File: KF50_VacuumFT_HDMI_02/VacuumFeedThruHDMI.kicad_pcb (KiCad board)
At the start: 4 copper layers, 112 x 151.5 mm, 16 parts, among them J1 HDMI_A_1.4, J2 HDMI_A_1.4, J3 HDMI_A_1.4, J4 HDMI_A_1.4, J5 HDMI_A_1.4, J6 HDMI_A_1.4, J7 HDMI_A_1.4, J8 HDMI_A_1.4, J9 HDMI_A_1.4, M1 DB25_Male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

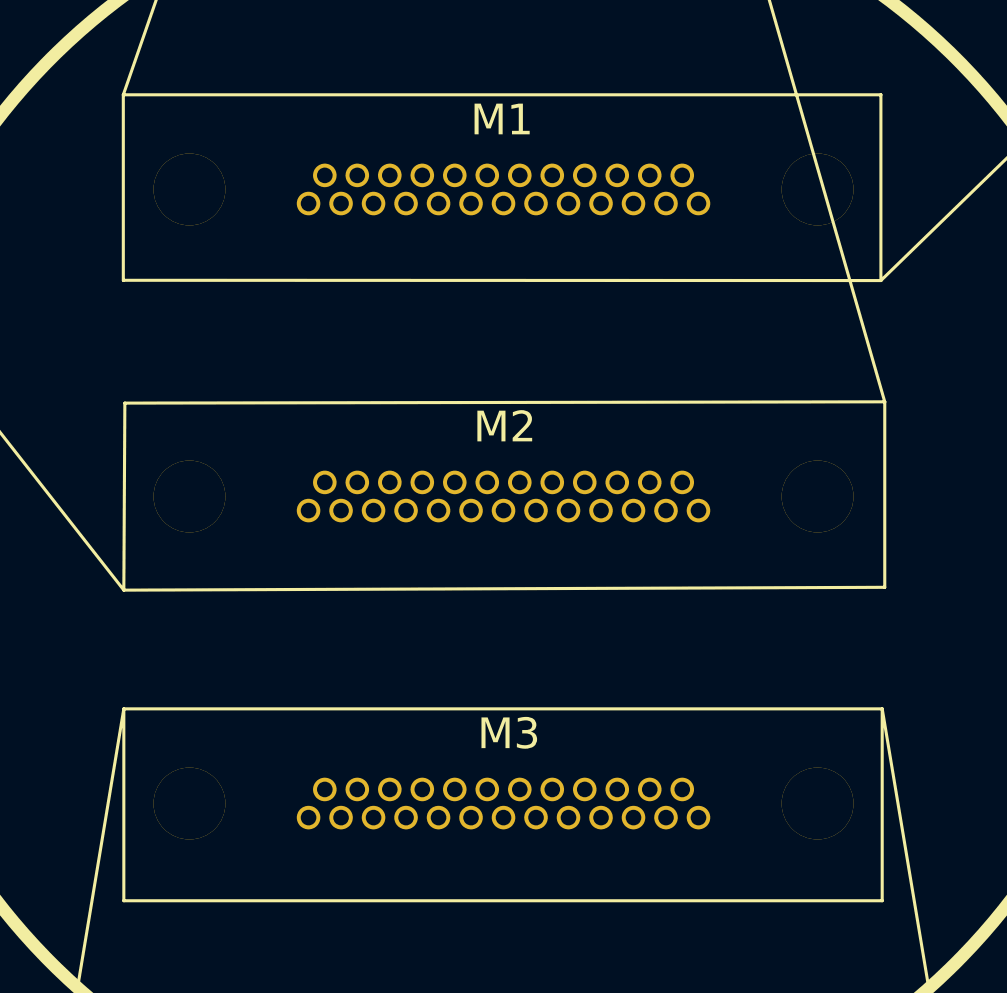
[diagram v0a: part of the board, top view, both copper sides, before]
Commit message: Update oring and removed microD holes
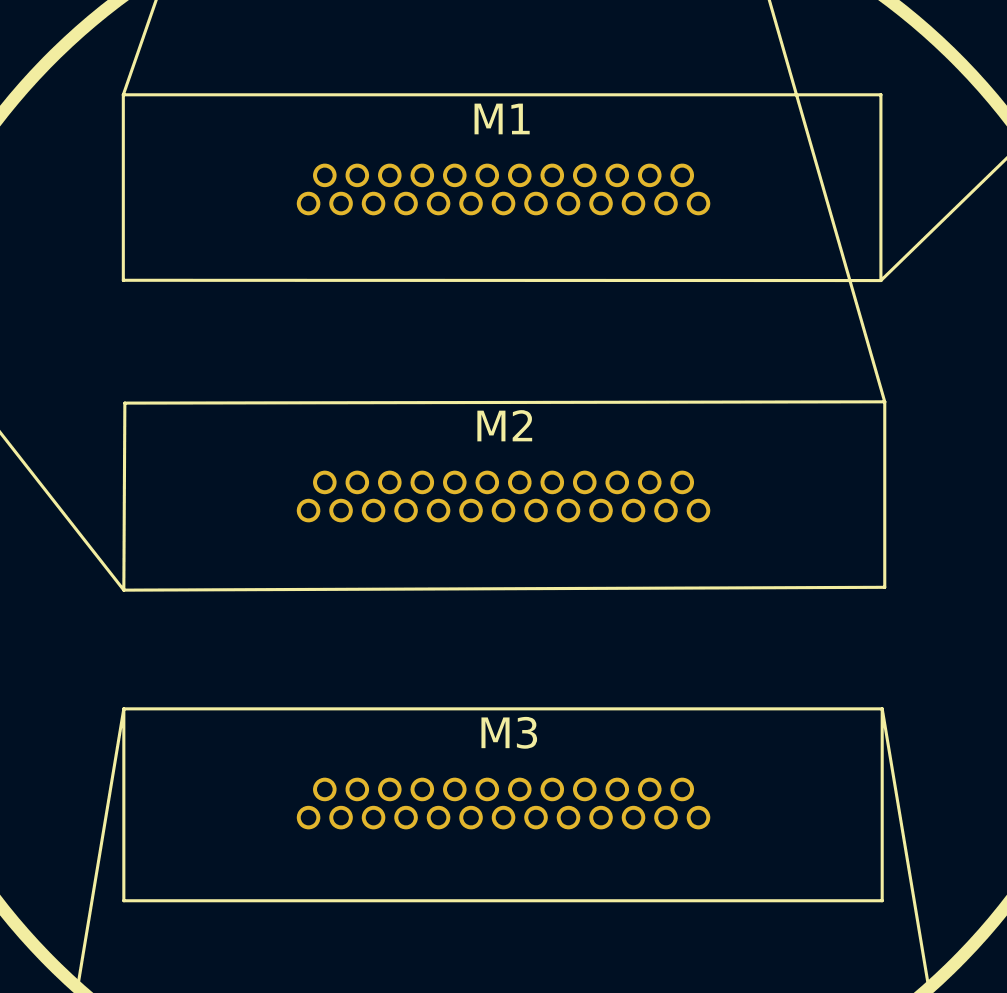
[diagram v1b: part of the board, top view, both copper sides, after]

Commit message: Fixed Trace to hole spacing
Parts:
- renumbered M2 to J13
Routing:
- net GND: track 368.3 -> 354.4 mm
- net Net-(J3-Pad12): track 84.3 -> 92.2 mm
- net Net-(J2-Pad12): track 69.6 -> 74.7 mm
- net Net-(J3-Pad3): track 80.6 -> 85.0 mm
- net Net-(J3-Pad6): track 82.0 -> 86.2 mm
- net Net-(J3-Pad4): track 81.5 -> 85.5 mm
- net Net-(J3-Pad10): track 84.5 -> 88.2 mm
- net Net-(J3-Pad1): track 80.4 -> 83.4 mm
- net Net-(J7-Pad10): track 65.5 -> 67.9 mm
- net Net-(J7-Pad12): track 67.9 -> 70.2 mm
- net Net-(J1-Pad9): track 54.0 -> 55.4 mm
- net Net-(J4-Pad7): track 87.1 -> 85.9 mm
- net Net-(J5-Pad3): track 77.3 -> 78.4 mm
- net Net-(J8-Pad7): track 97.6 -> 98.6 mm
- net Net-(J2-Pad9): track 66.4 -> 67.4 mm
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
